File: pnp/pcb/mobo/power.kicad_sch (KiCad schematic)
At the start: 31 parts, among them J12 COMBO_POWER_JACK, U11 FDS4435BZ, U12 TPS54331, U13 AP1117-33, U6 Fuse_Holder_3568

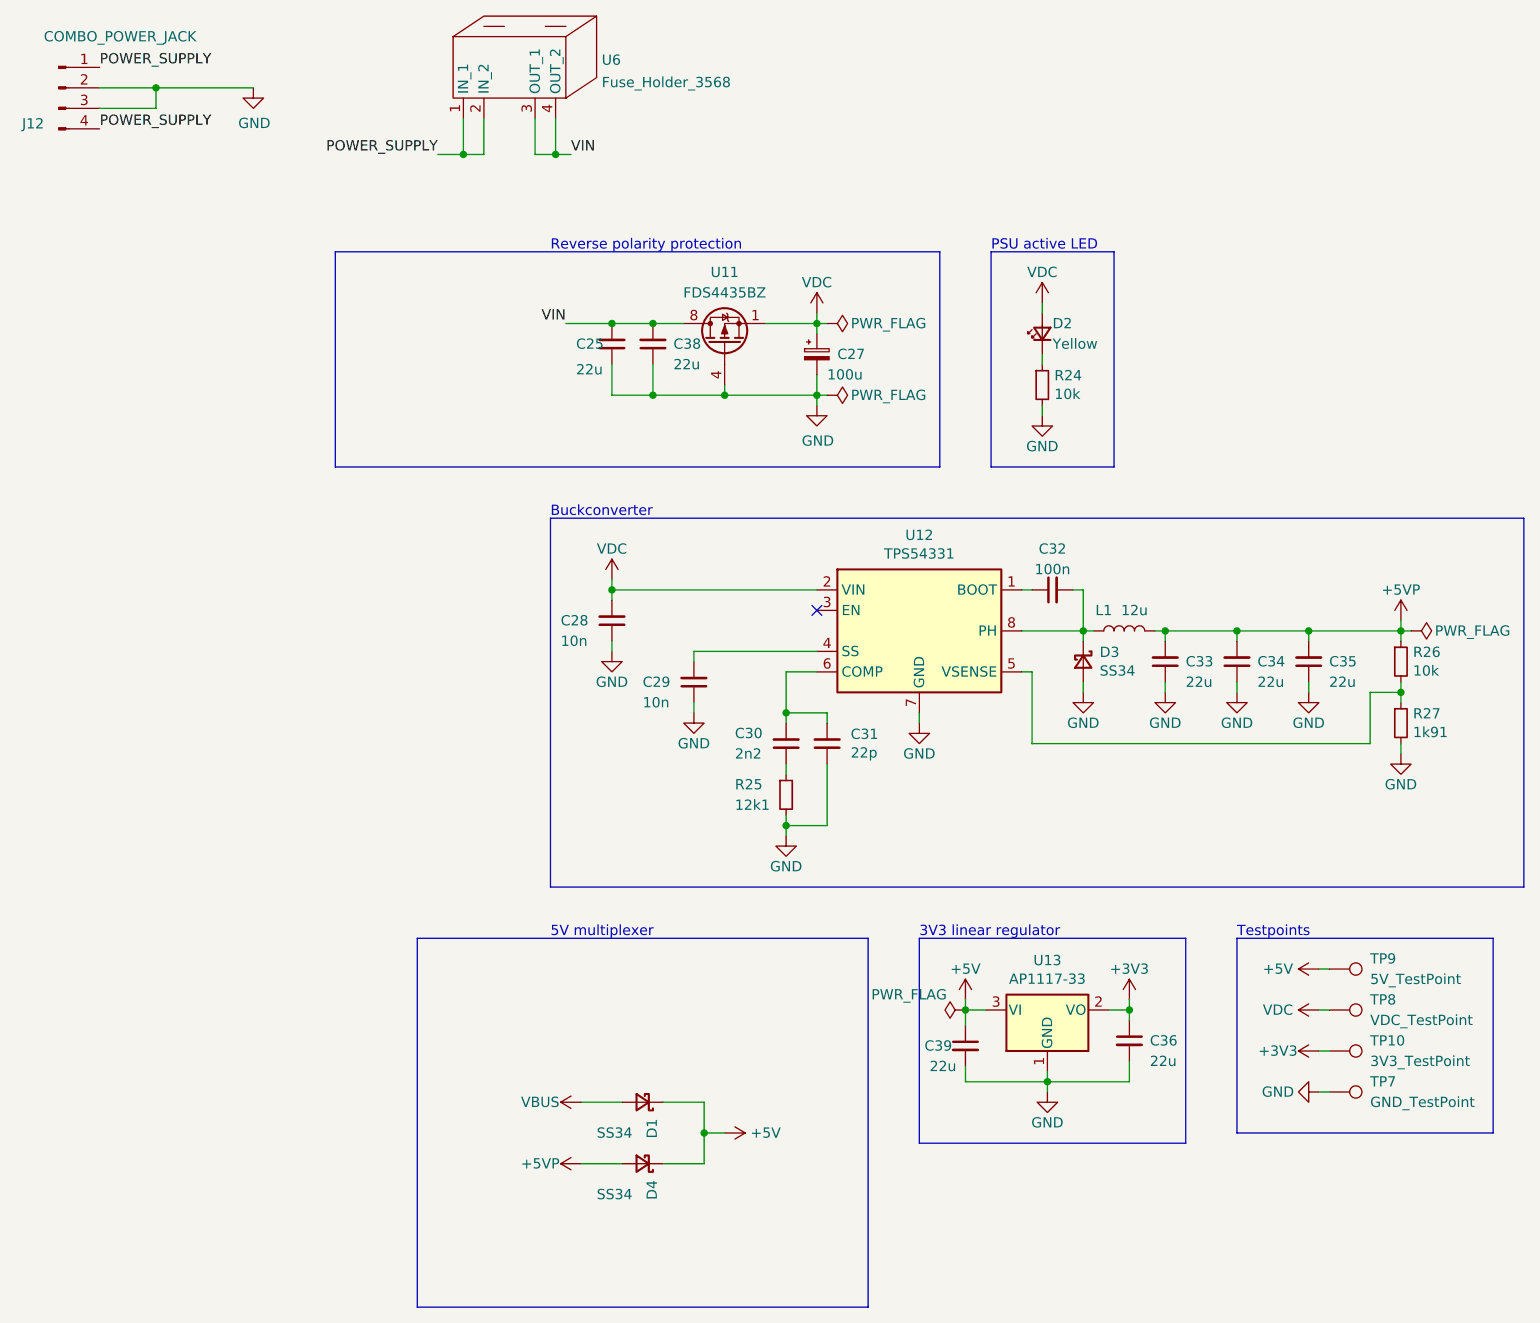
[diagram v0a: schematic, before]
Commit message: tweak PN of mobo
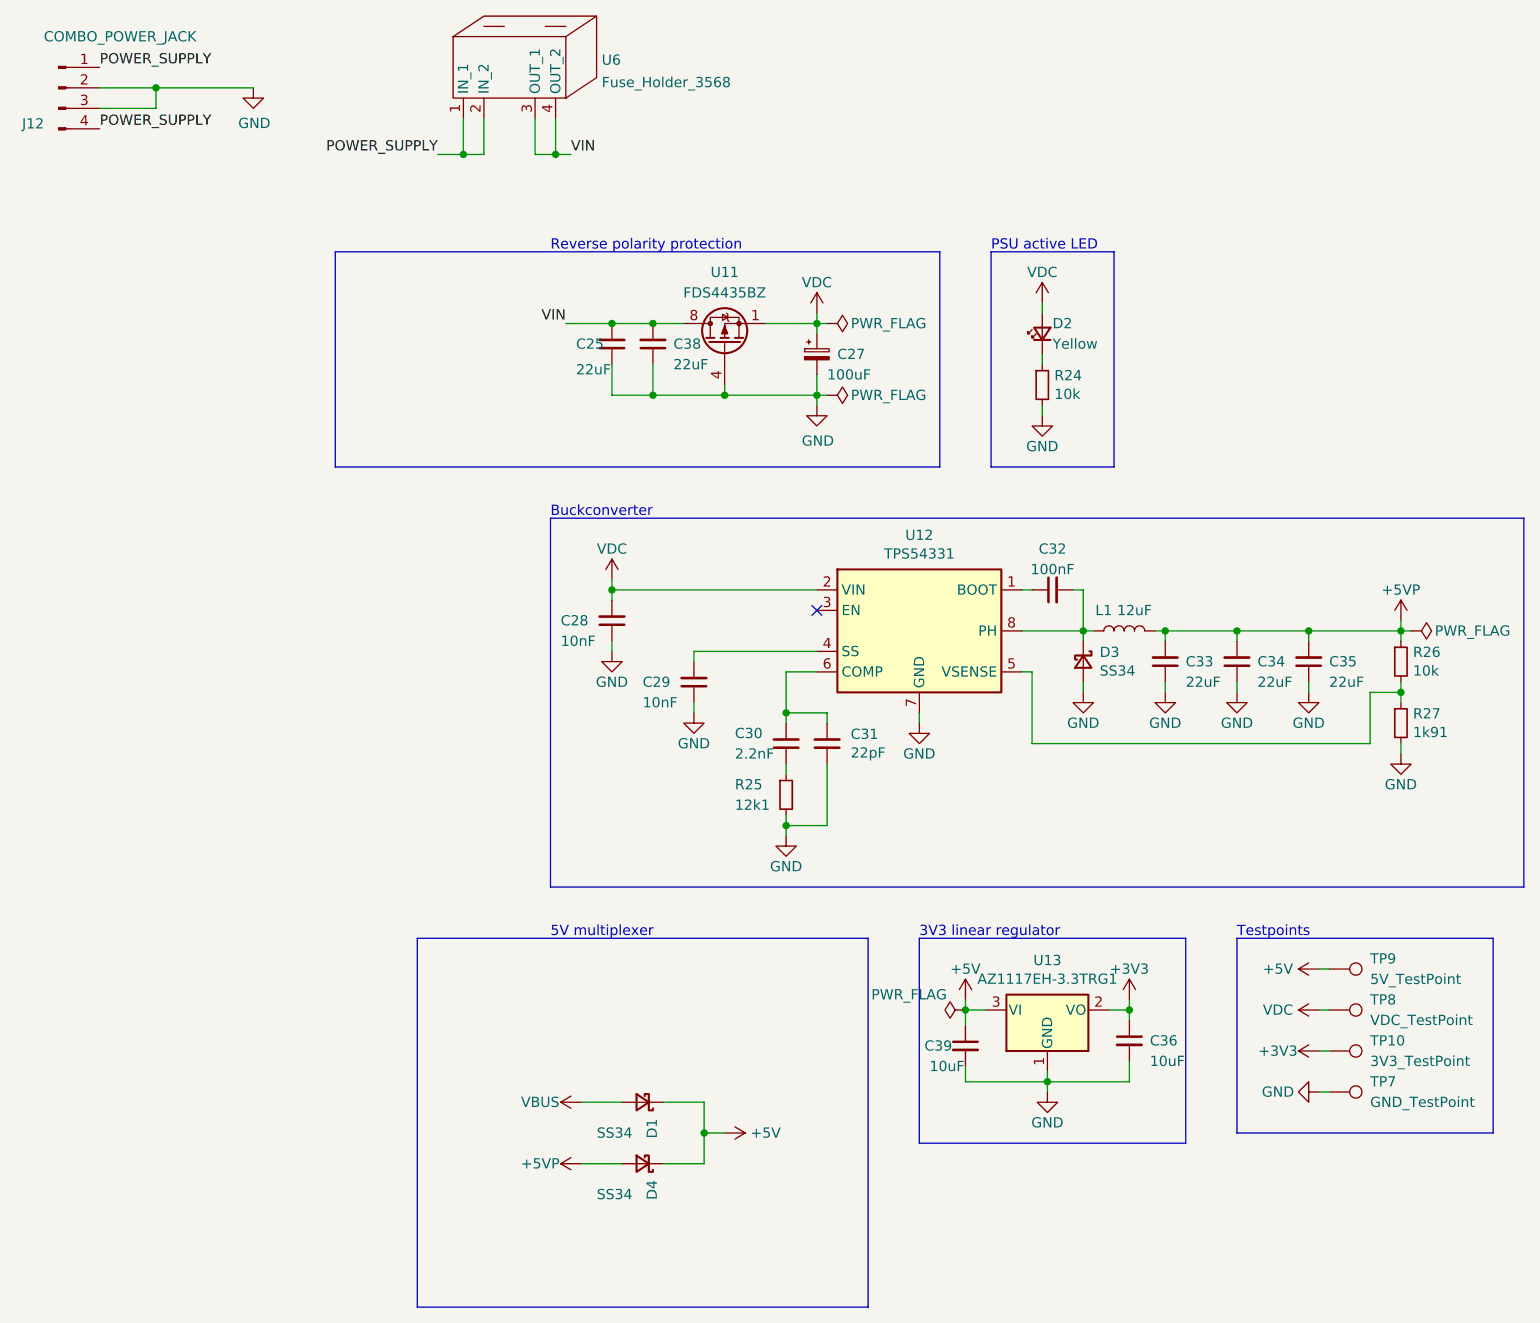
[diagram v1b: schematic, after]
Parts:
- C25, C33, C34, C35, C38: value 22u -> 22uF
- C27: value 100u -> 100uF
- C28, C29: value 10n -> 10nF
- C30: value 2n2 -> 2.2nF
- C31: value 22p -> 22pF
- C32: value 100n -> 100nF
- C36, C39: value 22u -> 10uF
- J12: LCSC (none) -> C16214
- L1: value 12u -> 12uF
- TP10, TP7, TP8, TP9: LCSC (none) -> DNP
- U13: value AP1117-33 -> AZ1117EH-3.3TRG1; Digikey ZLDO1117G33DICT-ND -> (none); JLCPCB C108785 -> (none); LCSC C108785 -> C108494; Mouser 522-ZLDO1117G33TA -> (none)
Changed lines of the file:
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@@
       (effects (font (size 1.27 1.27)) (justify left))
     )
-    (property "Value" "100u" (at 123.19 62.23 0)
+    (property "Value" "100uF" (at 123.19 62.23 0)
       (effects (font (size 1.27 1.27)) (justify left))
     )
@@
       (effects (font (size 1.27 1.27)))
     )
-    (property "Value" "12u" (at 161.29 91.44 90)
+    (property "Value" "12uF" (at 161.29 91.44 90)
       (effects (font (size 1.27 1.27)))
     )
@@
       (effects (font (size 1.27 1.27)) (justify right))
     )
-    (property "Value" "10n" (at 90.17 95.25 0)
+    (property "Value" "10nF" (at 90.17 95.25 0)
       (effects (font (size 1.27 1.27)) (justify right))
     )
@@
       (effects (font (size 1.27 1.27)))
     )
-    (property "Value" "AP1117-33" (at 150.495 137.1346 0)
+    (property "Value" "AZ1117EH-3.3TRG1" (at 150.495 137.1346 0)
       (effects (font (size 1.27 1.27)))
     )
@@
       (effects (font (size 1.27 1.27)) hide)
     )
-    (property "Datasheet" "http://www.diodes.com/datasheets/AP1117.pdf" (at 153.035 147.32 0)
-      (effects (font (size 1.27 1.27)) hide)
-    )
-    (property "JLCPCB" "C108785" (at 150.495 140.97 0)
-      (effects (font (size 1.27 1.27)) hide)
-    )
-    (property "LCSC" "C108785" (at 150.495 140.97 0)
+    (property "Datasheet" "" (at 153.035 147.32 0)
+      (effects (font (size 1.27 1.27)) hide)
+    )
+    (property "JLCPCB" "" (at 150.495 140.97 0)
+      (effects (font (size 1.27 1.27)) hide)
+    )
+    (property "LCSC" "C108494" (at 150.495 140.97 0)
       (effects (font (size 1.27 1.27)) hide)
     )
@@
       (effects (font (size 1.27 1.27)) hide)
     )
-    (property "Digikey" "ZLDO1117G33DICT-ND" (at 150.495 140.97 0)
-      (effects (font (size 1.27 1.27)) hide)
-    )
-    (property "Mouser" "522-ZLDO1117G33TA" (at 150.495 140.97 0)
+    (property "Digikey" "" (at 150.495 140.97 0)
+      (effects (font (size 1.27 1.27)) hide)
+    )
+    (property "Mouser" "" (at 150.495 140.97 0)
       (effects (font (size 1.27 1.27)) hide)
     )
@@
       (effects (font (size 1.27 1.27)) (justify left))
     )
-    (property "Value" "22u" (at 163.195 147.32 0)
+    (property "Value" "10uF" (at 163.195 147.32 0)
       (effects (font (size 1.27 1.27)) (justify left))
     )
@@
       (effects (font (size 1.27 1.27)))
     )
-    (property "Value" "100n" (at 151.13 86.36 90)
+    (property "Value" "100nF" (at 151.13 86.36 90)
       (effects (font (size 1.27 1.27)))
     )
@@
       (effects (font (size 1.27 1.27)) (justify right))
     )
-    (property "Value" "10n" (at 100.33 102.87 0)
+    (property "Value" "10nF" (at 100.33 102.87 0)
       (effects (font (size 1.27 1.27)) (justify right))
     )
@@
       (effects (font (size 1.27 1.27)) (justify right))
     )
-    (property "Value" "2n2" (at 111.76 109.22 0)
+    (property "Value" "2.2nF" (at 111.76 109.22 0)
       (effects (font (size 1.27 1.27)) (justify right))
     )
@@
       (effects (font (size 1.27 1.27)) (justify right))
     )
-    (property "Value" "22p" (at 126.111 109.093 0)
+    (property "Value" "22pF" (at 126.111 109.093 0)
       (effects (font (size 1.27 1.27)) (justify right))
     )
@@
       (effects (font (size 1.27 1.27)) (justify right))
     )
-    (property "Value" "22u" (at 185.42 100.33 0)
+    (property "Value" "22uF" (at 185.42 100.33 0)
       (effects (font (size 1.27 1.27)) (justify right))
     )
@@
       (effects (font (size 1.27 1.27)) (justify right))
     )
-    (property "Value" "22u" (at 176.53 100.33 0)
+    (property "Value" "22uF" (at 176.53 100.33 0)
       (effects (font (size 1.27 1.27)) (justify right))
     )
@@
       (effects (font (size 1.27 1.27)) (justify right))
     )
-    (property "Value" "22u" (at 167.64 100.33 0)
+    (property "Value" "22uF" (at 167.64 100.33 0)
       (effects (font (size 1.27 1.27)) (justify right))
     )
@@
       (effects (font (size 1.27 1.27)) hide)
     )
+    (property "LCSC" "DNP" (at 185.42 140.97 0)
+      (effects (font (size 1.27 1.27)) hide)
+    )
     (pin "1")
     (instances
@@
       (effects (font (size 1.27 1.27)) hide)
     )
+    (property "LCSC" "DNP" (at 185.42 135.89 0)
+      (effects (font (size 1.27 1.27)) hide)
+    )
     (pin "1")
     (instances
@@
       (effects (font (size 1.27 1.27)) hide)
     )
+    (property "LCSC" "DNP" (at 185.42 146.05 0)
+      (effects (font (size 1.27 1.27)) hide)
+    )
     (pin "1")
     (instances
@@
       (effects (font (size 1.27 1.27)) hide)
     )
+    (property "LCSC" "DNP" (at 185.42 151.13 0)
+      (effects (font (size 1.27 1.27)) hide)
+    )
     (pin "1")
     (instances
@@
       (effects (font (size 1.27 1.27)) (justify right))
     )
-    (property "Value" "22u" (at 92.075 61.595 0)
+    (property "Value" "22uF" (at 92.075 61.595 0)
       (effects (font (size 1.27 1.27)) (justify right))
     )
@@
       (effects (font (size 1.27 1.27)) (justify left))
     )
-    (property "Value" "22u" (at 135.89 147.955 0)
+    (property "Value" "10uF" (at 135.89 147.955 0)
       (effects (font (size 1.27 1.27)) (justify left))
     )
@@
       (effects (font (size 1.27 1.27)) (justify right))
     )
-    (property "Value" "22u" (at 104.14 60.96 0)
+    (property "Value" "22uF" (at 104.14 60.96 0)
       (effects (font (size 1.27 1.27)) (justify right))
     )
@@
       (effects (font (size 1.27 1.27)) hide)
     )
+    (property "LCSC" "C16214" (at 27.94 26.67 0)
+      (effects (font (size 1.27 1.27)) hide)
+    )
